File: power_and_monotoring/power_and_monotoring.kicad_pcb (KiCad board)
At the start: 2 copper layers, 122 x 177 mm, 149 parts, among them IC1 ADP3335ARMZ-5-R7, IC2 ADP3335ARMZ-3.3-RL, J1 Microfit_01x02_Vertical, J2 HLE-108-02-L-DV-BE-K-TR, J3 HLE-108-02-L-DV-BE-K-TR, J4 HLE-108-02-L-DV-BE-K-TR, J5 HLE-108-02-L-DV-BE-K-TR, K1 G5Q-1A, K2 G5Q-1A, K3 G5Q-1A, Q1 DMN6075SQ-7, U10 P783-Q24-S3-S, U11 CD4051BM96G3, U12 CD4051BM96G3, U2 LM7902D, U3 LM7902D, U4 LM7902D, U6 CD4081BM96, U7 CD4071BM96

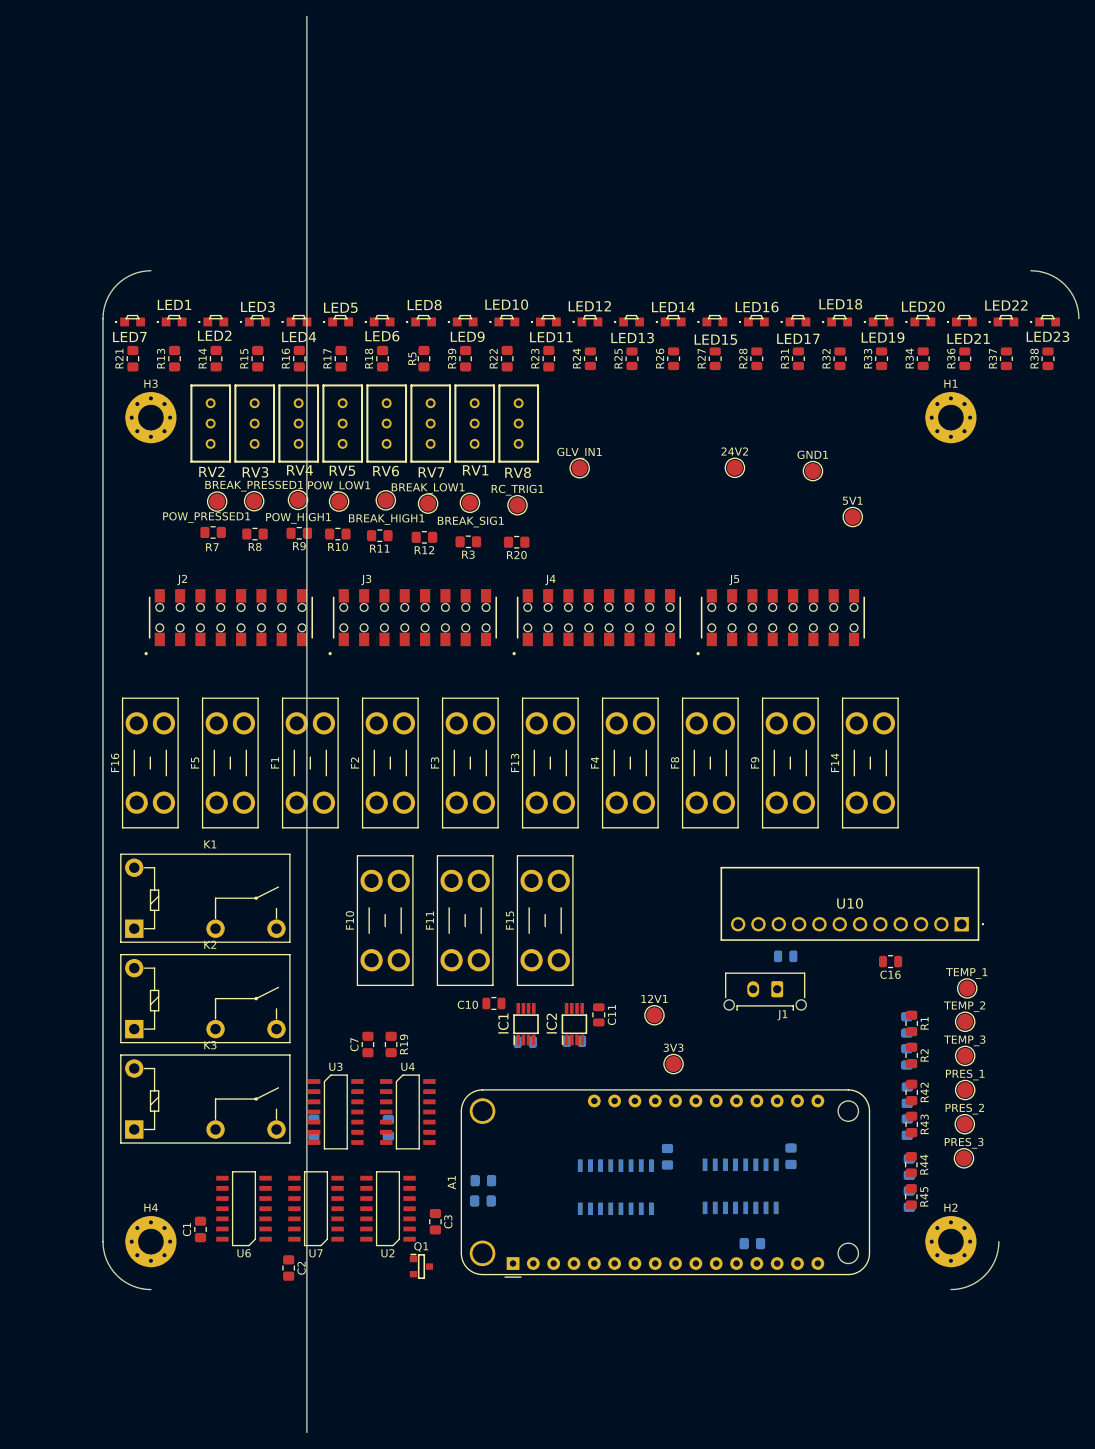
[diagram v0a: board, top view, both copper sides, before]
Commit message: first connections done (not perfect yet)
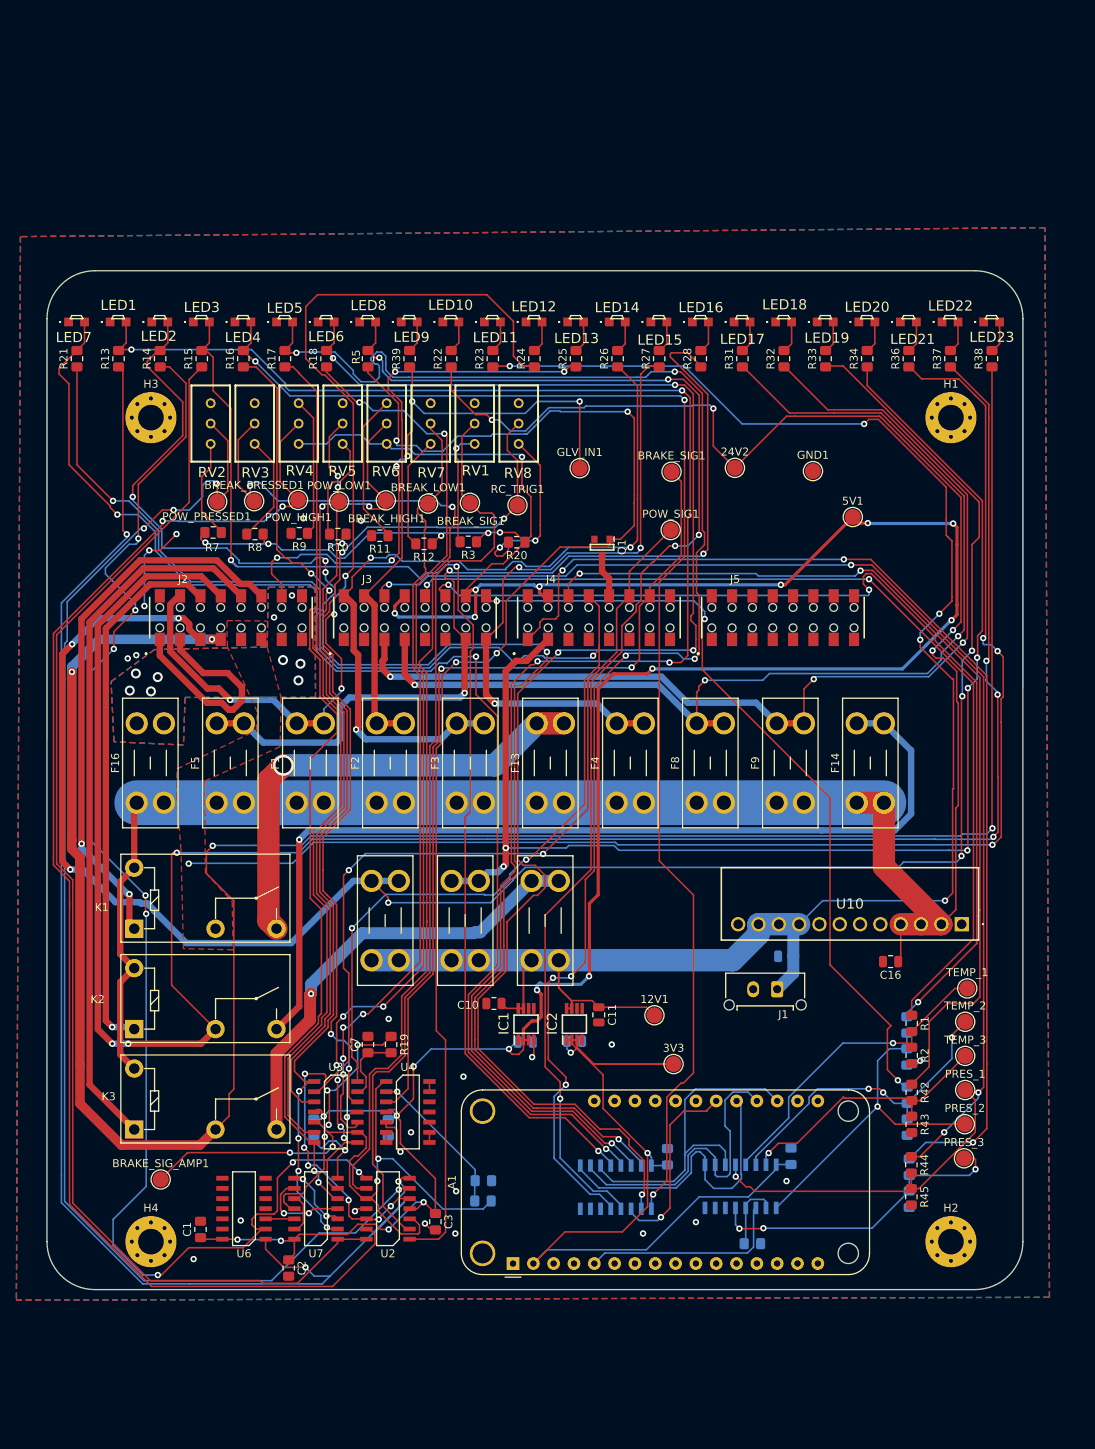
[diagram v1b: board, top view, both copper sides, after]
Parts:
- added BRAKE_SIG1: TestPoint, TestPoint:TestPoint_Pad_D2.0mm, F.Cu at (119.4, 151.9)
- added BRAKE_SIG_AMP1: TestPoint, TestPoint:TestPoint_Pad_D2.0mm, F.Cu at (55.5, 240.4)
- added POW_SIG1: TestPoint, TestPoint:TestPoint_Pad_D2.0mm, F.Cu at (119.3, 159.2)
- R24, R25, R26, R27, R28, R31, R32, R33, R34, R36, R37, R38: footprint Resistor_SMD:R_0805_2012Metric -> UniSA_Motorsport_Resistor:0805
- moved Q1 92.7 mm to (110.7, 161.4), turned to -90 degrees
- moved LED1 7.00 mm to (50.2, 133.2)
- moved LED10 7.00 mm to (91.8, 133.2)
- moved LED11 7.00 mm to (97.0, 133.2)
- moved LED12 7.00 mm to (102.2, 133.2)
- moved LED13 7.00 mm to (107.4, 133.2)
- moved LED14 7.00 mm to (112.6, 133.2)
- moved LED15 7.00 mm to (117.8, 133.2)
- moved LED17 7.00 mm to (128.2, 133.2)
- moved LED18 7.00 mm to (133.4, 133.2)
- moved LED19 7.00 mm to (138.6, 133.2)
- moved LED2 7.00 mm to (55.4, 133.2)
- moved LED20 7.00 mm to (143.8, 133.2)
- moved LED21 7.00 mm to (149.0, 133.2)
- moved LED22 7.00 mm to (154.2, 133.2)
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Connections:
- J2 pad 11: /Connectors/RADIATOR_FAN_24V -> /Connectors/RADIATOR_WATER_PUMP_24V
- J2 pad 8: /Connectors/RADIATOR_WATER_PUMP_24V -> /Connectors/RADIATOR_FAN_24V
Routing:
- net +5V: track 0.00 -> 394.6 mm, vias 0 -> 26
- net +24V: track 0.00 -> 301.6 mm, vias 0 -> 4
- net /Connectors/MC_12V: track 0.00 -> 289.3 mm, vias 0 -> 4
- net /Connectors/RADIATOR_FAN_24V: track 0.00 -> 275.3 mm, vias 0 -> 6
- net /Connectors/BRAKE_LIGHT_12V: track 0.00 -> 245.3 mm, vias 0 -> 7
- net +12V: track 0.00 -> 230.6 mm, vias 0 -> 5
- net /feather/POWER_SIG_HIGH: track 0.00 -> 208.4 mm, vias 0 -> 5
- net /feather/BRAKE_SIG_AMP_SHORT_GND: track 0.00 -> 192.8 mm, vias 0 -> 5
- net /feather/BRAKE_SIG_AMP_SHORT_HIGH: track 0.00 -> 189.1 mm, vias 0 -> 7
- net Net-(R13-Pad1): track 0.00 -> 186.0 mm, vias 0 -> 3
- net /feather/BRAKE_SIG_AMP_HIGH: track 0.00 -> 181.1 mm, vias 0 -> 5
- net /Connectors/BSPD_TRIGGER: track 0.00 -> 180.0 mm, vias 0 -> 4
- net Net-(R14-Pad1): track 0.00 -> 171.4 mm, vias 0 -> 8
- net /Connectors/RADIATOR_WATER_PUMP_24V: track 0.00 -> 170.6 mm, vias 0 -> 4
- net Net-(U2D--): track 0.00 -> 168.6 mm, vias 0 -> 2
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- added copper zone on B.Cu, net /Connectors/GLV_MASTER_SWITCH_OUT
- added copper zone on F.Cu, net /Connectors/GLV_MASTER_SWITCH_OUT
- added copper zone on F.Cu, net /Connectors/RADIATOR_WATER_PUMP_24V
- added copper zone on B.Cu, net GND
- added copper zone on F.Cu, net GND
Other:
- board size 122 x 177 mm -> 122 x 127.4 mm

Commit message: before design review
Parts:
- removed LED1, LED2, LED3, LED4, LED5, LED6, LED7: RED, LTST-S270KRKT, UniSA_Motorsport_Diode:0605
- removed LED10, LED11, LED12, LED13, LED14, LED15, LED16, LED17, LED18, LED19, LED20, LED21, LED22, LED23, LED8, LED9: GREEN, LTST-S270KGKT, UniSA_Motorsport_Diode:0605
- removed RV1, RV2, RV3, RV4, RV5, RV6, RV7, RV8: 10K, UniSA_Motorsport_Others:3296X_POT
- added D1: RED, UniSA_Motorsport_Diode:0805, F.Cu at (50.1, 134.2)
- added D10: GREEN, UniSA_Motorsport_Diode:0805, F.Cu at (92.0, 134.2)
- added D11: GREEN, UniSA_Motorsport_Diode:0805, F.Cu at (97.2, 134.2)
- added D12: GREEN, UniSA_Motorsport_Diode:0805, F.Cu at (102.4, 134.2)
- added D13: GREEN, UniSA_Motorsport_Diode:0805, F.Cu at (107.6, 134.2)
- added D14: GREEN, UniSA_Motorsport_Diode:0805, F.Cu at (112.8, 134.2)
- added D15: GREEN, UniSA_Motorsport_Diode:0805, F.Cu at (118.0, 134.2)
- added D16: GREEN, UniSA_Motorsport_Diode:0805, F.Cu at (123.2, 134.2)
- added D17: GREEN, UniSA_Motorsport_Diode:0805, F.Cu at (128.4, 134.2)
- added D18: GREEN, UniSA_Motorsport_Diode:0805, F.Cu at (133.6, 134.2)
- added D19: GREEN, UniSA_Motorsport_Diode:0805, F.Cu at (138.8, 134.2)
- added D2: RED, UniSA_Motorsport_Diode:0805, F.Cu at (55.6, 134.2)
- added D20: GREEN, UniSA_Motorsport_Diode:0805, F.Cu at (144.0, 134.2)
- added D21: GREEN, UniSA_Motorsport_Diode:0805, F.Cu at (149.2, 134.2)
- added D22: GREEN, UniSA_Motorsport_Diode:0805, F.Cu at (154.4, 134.2)
- added D23: GREEN, UniSA_Motorsport_Diode:0805, F.Cu at (159.6, 134.2)
- added D3: RED, UniSA_Motorsport_Diode:0805, F.Cu at (60.8, 134.2)
- added D4: RED, UniSA_Motorsport_Diode:0805, F.Cu at (66.0, 134.2)
- added D5: RED, UniSA_Motorsport_Diode:0805, F.Cu at (71.2, 134.2)
- added D6: RED, UniSA_Motorsport_Diode:0805, F.Cu at (76.4, 134.2)
- added D7: RED, UniSA_Motorsport_Diode:0805, F.Cu at (44.6, 134.2)
- added D8: GREEN, UniSA_Motorsport_Diode:0805, F.Cu at (81.6, 134.2)
- added D9: GREEN, UniSA_Motorsport_Diode:0805, F.Cu at (86.8, 134.2)
- added J6: 43045-1015, UniSA_Motorsport_Connector:MOLEX_43045-10YY_10PIN, F.Cu at (151.4, 168.8)
- added J7: 43045-1615, UniSA_Motorsport_Connector:MOLEX_43045-16YY_16PIN, F.Cu at (131.0, 150.4)
- added RL1: 10 K, UniSA_Motorsport_Resistor:3296W-1, F.Cu at (61.7, 145.9)
- added RL2: 10 K, UniSA_Motorsport_Resistor:3296W-1, F.Cu at (67.3, 145.9)
- added RL3: 10 K, UniSA_Motorsport_Resistor:3296W-1, F.Cu at (72.9, 146.0)
- added RL4: 10 K, UniSA_Motorsport_Resistor:3296W-1, F.Cu at (78.2, 146.0)
- added RL5: 10 K, UniSA_Motorsport_Resistor:3296W-1, F.Cu at (83.7, 145.8)
- added RL6: 10 K, UniSA_Motorsport_Resistor:3296W-1, F.Cu at (89.6, 145.9)
- added RL7: 10 K, UniSA_Motorsport_Resistor:3296W-1, F.Cu at (100.5, 146.0)
- added RL8: 10 K, UniSA_Motorsport_Resistor:3296W-1, F.Cu at (95.0, 145.9)
- moved 5V1 27.8 mm to (153.0, 183.1)
- moved 24V2 17.7 mm to (110.0, 147.6)
- moved GND1 15.6 mm to (152.6, 153.6)
- moved BRAKE_SIG1 8.24 mm to (111.2, 152.3)
- moved Q1 3.59 mm to (110.8, 157.8)
- moved R12 1.83 mm to (88.6, 159.1)
- moved R3 1.08 mm to (94.1, 159.6)
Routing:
- net /feather/D_BSPD_TRIGGER: track 165.2 -> 310.6 mm, vias 3 -> 5
- net /feather/BRAKE_LIGHT_SIG: track 164.6 -> 247.8 mm, vias 5 -> 6
- net /feather/BRAKE_SIG_AMP_SHORT_HIGH: track 189.1 -> 269.3 mm, vias 7 -> 10
- net /feather/POWER_SIG_SHORT_GND: track 168.2 -> 241.5 mm, vias 3 -> 7
- net /feather/BRAKE_SIG_AMP_SHORT_GND: track 192.8 -> 265.4 mm, vias 5 -> 6
- net /feather/POWER_SIG_HIGH: track 208.4 -> 279.3 mm, vias 5 -> 6
- net /feather/POWER_SIG_SHORT_HIGH: track 149.5 -> 211.2 mm, vias 3 -> 5
- net /Connectors/BSPD_TEST_12V: track 164.1 -> 113.6 mm
- net /feather/BRAKE_SIG_AMP_HIGH: track 181.1 -> 231.4 mm, vias 5 -> 6
- net /Connectors/SAFETY_24V: track 74.0 -> 122.0 mm, vias 2 -> 3
- net /Connectors/AIR_24V: track 123.9 -> 171.1 mm, vias 4 -> 8
- net /Connectors/ECU_24V: track 139.4 -> 98.8 mm
- net /Connectors/MC_12V: track 289.3 -> 324.4 mm, vias 4 -> 7
- net /Connectors/RADIATOR_FAN_24V: track 275.3 -> 306.5 mm
- net /Connectors/BRAKE_LIGHT_12V: track 245.3 -> 273.2 mm, vias 7 -> 8
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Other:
- board size 122 x 127.4 mm -> 122 x 124.4 mm
- board text added: "12 Break light"
- board text added: "12V motor controller"
- board text added: "AIR 24V"
- board text added: "B1-1"
- board text added: "B1-10"
- board text added: "B1-11"
- board text added: "B1-12"
- board text added: "B1-13"
- board text added: "B1-14"
- board text added: "B1-15"
- board text added: "B1-16"
- board text added: "B1-2"
- board text added: "B1-3"
- board text added: "B1-4"
- board text added: "B1-5"
- board text added: "B1-6"
- board text added: "B1-7"
- board text added: "B1-8"
- board text added: "B1-9"
- board text added: "B2-1"
- board text added: "B2-10"
- board text added: "B2-11"
- board text added: "B2-12"
- board text added: "B2-13"
- board text added: "B2-14"
- board text added: "B2-15"
- board text added: "B2-16"
- board text added: "B2-2"
- board text added: "B2-3"
- board text added: "B2-4"
- board text added: "B2-5"
- board text added: "B2-6"
- board text added: "B2-7"
- board text added: "B2-8"
- board text added: "B2-9"
- board text added: "B3-1"
- board text added: "B3-10"
- board text added: "B3-11"
- board text added: "B3-12"
- board text added: "B3-13"
- board text added: "B3-14"
- board text added: "B3-15"
- board text added: "B3-16"
- board text added: "B3-2"
- board text added: "B3-3"
- board text added: "B3-4"
- board text added: "B3-5"
- board text added: "B3-6"
- board text added: "B3-7"
- board text added: "B3-8"
- board text added: "B3-9"
- board text added: "B4-1"
- board text added: "B4-10"
- board text added: "B4-11"
- board text added: "B4-12"
- board text added: "B4-13"
- board text added: "B4-14"
- board text added: "B4-15"
- board text added: "B4-16"
- board text added: "B4-2"
- board text added: "B4-3"
- board text added: "B4-4"
- board text added: "B4-5"
- board text added: "B4-6"
- board text added: "B4-7"
- board text added: "B4-8"
- board text added: "B4-9"
- board text added: "BSPD 12V"
- board text added: "Dash 24V"
- board text added: "ECU 24V"
- board text added: "GLV IN"
- board text added: "HV BOX 24V"
- board text added: "M ACC 24V"
- board text added: "POWER SIG"
- board text added: "Radiator Pump"
- board text added: "Radiator fan"
- board text added: "S ACC 24V"
- board text added: "SAFTEY 24V"

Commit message: Final
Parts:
- removed C1: GCM0805_1u, UniSA_Motorsport_Capacitor:0805
- removed C16, C17: C, Capacitor_SMD:C_0805_2012Metric
- removed R10, R11, R12, R20, R35, R41, R42, R43, R9: CRCW0805, UniSA_Motorsport_Resistor:0805
- removed U10: P783-Q24-S3-S, UniSA_Motorsport_Others:P783-Q24-S3-S
- removed U6: CD4081BM96, UniSA_Motorsport_SO:SOIC-14
- added C6: 100uF, UniSA_Motorsport_Capacitor:EEEFK0J332AQ, F.Cu at (146.2, 206.2)
- added C8: EEV-FK1H391Q, UniSA_Motorsport_Capacitor:EEEFK0J332AQ, F.Cu at (127.3, 206.7)
- added D24: 1N4148W RHG, UniSA_Motorsport_Diode:SOD-123F-2, F.Cu at (74.7, 203.2)
- added D25: 1N4148W RHG, UniSA_Motorsport_Diode:SOD-123F-2, F.Cu at (74.8, 210.2)
- added D26: 1N4148W RHG, UniSA_Motorsport_Diode:SOD-123F-2, F.Cu at (48.8, 241.4)
- added D27: NRVTS245ESFT1G, UniSA_Motorsport_Diode:SOD-123FL-2, F.Cu at (119.3, 222.9)
- added D28: MMBZ5225BS-7-F, UniSA_Motorsport_SOT_TO:SOT-363, B.Cu at (99.3, 236.6)
- added D29: MMBZ5225BS-7-F, UniSA_Motorsport_SOT_TO:SOT-363, B.Cu at (101.2, 227.0)
- added D30: MMBZ5225BS-7-F, UniSA_Motorsport_SOT_TO:SOT-363, B.Cu at (122.8, 219.0)
- added D31: MMBZ5225BS-7-F, UniSA_Motorsport_SOT_TO:SOT-363, B.Cu at (122.7, 215.8)
- added IC3: LM2576-12WU-TR, UniSA_Motorsport_SO:TO-263-5, F.Cu at (145.4, 221.1)
- added L1: 100uH, UniSA_Motorsport_Inductor:5050, F.Cu at (128.0, 222.1)
- added R29: CRCW0805, UniSA_Motorsport_Resistor:0805, F.Cu at (88.0, 238.3)
- added R30: CRCW0805, UniSA_Motorsport_Resistor:0805, F.Cu at (89.6, 241.1)
- added R50: CRCW0805, UniSA_Motorsport_Resistor:0805, F.Cu at (93.4, 227.0)
- added R51: CRCW0805, UniSA_Motorsport_Resistor:0805, F.Cu at (93.4, 229.3)
- added RN1: EXB-38V103JV, UniSA_Motorsport_Resistor:EXB38V472JV, F.Cu at (92.8, 220.3)
- added RN2: EXB-38V103JV, UniSA_Motorsport_Resistor:EXB38V472JV, F.Cu at (114.6, 214.8)
- added U1: 74LVC1G08GW,125, UniSA_Motorsport_SO:TSSOP-5, F.Cu at (66.9, 250.9)
- R1, R2, R8: moved to B.Cu
- moved R8 110.2 mm to (147.1, 235.7), turned to 0 degrees
- moved POW_SIG_AMP1 100.1 mm to (59.8, 239.8)
- moved R7 83.7 mm to (68.4, 243.0), turned to 90 degrees
- moved R3 61.8 mm to (83.8, 220.5)
- moved BRAKE_SIG_AMP1 31.7 mm to (84.8, 252.5)
- moved R46 25.2 mm to (160.7, 243.3)
- moved R47 25.2 mm to (160.7, 247.3)
- moved J1 22.2 mm to (113.8, 204.8), turned to -90 degrees
- moved TEMP_2 16.2 mm to (150.8, 236.0)
- moved TEMP_3 16.2 mm to (150.8, 240.2)
- moved TEMP_1 16.2 mm to (151.0, 231.8)
- moved R2 14.9 mm to (143.8, 238.7), turned to 0 degrees
- moved R1 11.4 mm to (147.4, 232.2), turned to 0 degrees
- moved 12V1 7.90 mm to (116.6, 227.7)
- moved 3V3 6.81 mm to (113.0, 227.6)
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- renumbered D7 to D1, D1 to D2, D2 to D3, D3 to D4, D4 to D5, D5 to D6, D6 to D7, POW_SIG1 to POW_SIG_AMP1
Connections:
- C5 pad 1: +5V -> +12V
- D1 pad 2: /feather/D_BSPD_TRIGGER -> Net-(D1-A)
- D2 pad 2: /feather/POWER_SIG_HIGH -> Net-(D2-A)
- D3 pad 2: /feather/BRAKE_SIG_AMP_HIGH -> Net-(D3-A)
- D4 pad 2: /feather/POWER_SIG_SHORT_HIGH -> Net-(D4-A)
- D5 pad 2: /feather/POWER_SIG_SHORT_GND -> Net-(D5-A)
- D6 pad 2: /feather/BRAKE_SIG_AMP_SHORT_HIGH -> Net-(D6-A)
- D7 pad 2: /feather/BRAKE_SIG_AMP_SHORT_GND -> Net-(D7-A)
- D8 pad 2: /feather/BRAKE_LIGHT_SIG -> Net-(D8-A)
- J6 pad 7: /feather/D_BSPD_TRIGGER -> /Connectors/BSPD_TRIGGER
- POW_SIG_AMP1 pad 1: /Connectors/POWER_SIGNAL -> /logic/POW_SIG_AMP
- Q1 pad 1: Net-(Q1-G) -> /feather/BRAKE_LIGHT_SIG
- R1 pad 1: /Connectors/PRESSURE/TEMP_SENSOR_1_TEMP -> +3V3
- R1 pad 2: Net-(U12-X0) -> /Connectors/PRESSURE/TEMP_SENSOR_1_TEMP
- R13 pad 1: Net-(R13-Pad1) -> /feather/POWER_SIG_HIGH
- R13 pad 2: /feather/POWER_SIG_HIGH -> Net-(D2-A)
- R14 pad 1: Net-(R14-Pad1) -> /feather/BRAKE_SIG_AMP_HIGH
- R14 pad 2: /feather/BRAKE_SIG_AMP_HIGH -> Net-(D3-A)
- R15 pad 1: Net-(R15-Pad1) -> /feather/POWER_SIG_SHORT_HIGH
- R15 pad 2: /feather/POWER_SIG_SHORT_HIGH -> Net-(D4-A)
- R16 pad 1: Net-(R16-Pad1) -> /feather/POWER_SIG_SHORT_GND
- R16 pad 2: /feather/POWER_SIG_SHORT_GND -> Net-(D5-A)
- R17 pad 1: Net-(R17-Pad1) -> /feather/BRAKE_SIG_AMP_SHORT_HIGH
- R17 pad 2: /feather/BRAKE_SIG_AMP_SHORT_HIGH -> Net-(D6-A)
- R18 pad 1: Net-(R18-Pad1) -> /feather/BRAKE_SIG_AMP_SHORT_GND
- R18 pad 2: /feather/BRAKE_SIG_AMP_SHORT_GND -> Net-(D7-A)
- R2 pad 1: Net-(U12-X0) -> +3V3
- R2 pad 2: GND -> /Connectors/PRESSURE/TEMP_SENSOR_3_TEMP
- R21 pad 2: /feather/D_BSPD_TRIGGER -> Net-(D1-A)
- R3 pad 1: +5V -> Net-(R19-Pad1)
- R3 pad 2: Net-(R3-Pad2) -> GND
- R5 pad 1: Net-(Q1-G) -> /feather/BRAKE_LIGHT_SIG
- R5 pad 2: /feather/BRAKE_LIGHT_SIG -> Net-(D8-A)
- R6 pad 1: /logic/BRAKE_SIG_AMP -> Net-(R50-Pad1)
- R7 pad 1: +5V -> Net-(R7-Pad1)
- R7 pad 2: Net-(R7-Pad2) -> Net-(R19-Pad1)
- R8 pad 1: +5V -> +3V3
- R8 pad 2: Net-(R8-Pad2) -> /Connectors/PRESSURE/TEMP_SENSOR_2_TEMP
- RL1 pad 1: Net-(R7-Pad2) -> +3V3
- RL2 pad 1: Net-(R8-Pad2) -> +3V3
- RL3 pad 1: +5V -> +3V3
- RL3 pad 3: Net-(R9-Pad1) -> GND
- RL4 pad 1: Net-(R10-Pad2) -> +3V3
- RL5 pad 1: +5V -> +3V3
- RL5 pad 3: Net-(R11-Pad1) -> GND
- RL6 pad 1: Net-(R12-Pad2) -> +3V3
- RL7 pad 1: Net-(R20-Pad2) -> +3V3
- RL8 pad 1: Net-(R3-Pad2) -> +3V3
- TEMP_1 pad 1: Net-(U12-X0) -> /Connectors/PRESSURE/TEMP_SENSOR_1_TEMP
- TEMP_2 pad 1: Net-(U12-X1) -> /Connectors/PRESSURE/TEMP_SENSOR_2_TEMP
- TEMP_3 pad 1: Net-(U12-X2) -> /Connectors/PRESSURE/TEMP_SENSOR_3_TEMP
- U11 pad 1: /feather/POWER_SIG_SHORT_GND -> Net-(U11-X4)
- U11 pad 12: /feather/POWER_SIG_SHORT_HIGH -> Net-(U11-X3)
- U11 pad 13: /feather/D_BSPD_TRIGGER -> Net-(U11-X0)
- U11 pad 14: /feather/POWER_SIG_HIGH -> Net-(U11-X1)
- U11 pad 15: /feather/BRAKE_SIG_AMP_HIGH -> Net-(U11-X2)
- U11 pad 2: /feather/BRAKE_SIG_AMP_SHORT_GND -> Net-(U11-X6)
- U11 pad 4: /feather/BRAKE_LIGHT_SIG -> Net-(U11-X7)
- U11 pad 5: /feather/BRAKE_SIG_AMP_SHORT_HIGH -> Net-(U11-X5)
- U12 pad 13: Net-(U12-X0) -> /Connectors/PRESSURE/TEMP_SENSOR_1_TEMP
- U12 pad 14: Net-(U12-X1) -> /Connectors/PRESSURE/TEMP_SENSOR_2_TEMP
- U12 pad 15: Net-(U12-X2) -> /Connectors/PRESSURE/TEMP_SENSOR_3_TEMP
- U2 pad 1: Net-(Q1-G) -> /feather/BRAKE_LIGHT_SIG
- U2 pad 12: /Connectors/POWER_SIGNAL -> /logic/POW_SIG_AMP
- U2 pad 14: Net-(R15-Pad1) -> /feather/POWER_SIG_SHORT_HIGH
- U2 pad 5: /Connectors/POWER_SIGNAL -> /logic/POW_SIG_AMP
- U2 pad 7: Net-(R13-Pad1) -> /feather/POWER_SIG_HIGH
- U2 pad 8: Net-(R14-Pad1) -> /feather/BRAKE_SIG_AMP_HIGH
- U3 pad 1: Net-(R16-Pad1) -> /feather/POWER_SIG_SHORT_GND
- U3 pad 2: /Connectors/POWER_SIGNAL -> /logic/POW_SIG_AMP
- U3 pad 7: Net-(R17-Pad1) -> /feather/BRAKE_SIG_AMP_SHORT_HIGH
- U3 pad 8: Net-(R18-Pad1) -> /feather/BRAKE_SIG_AMP_SHORT_GND
- U4 pad 1: /logic/BRAKE_SIG_AMP -> Net-(R50-Pad1)
- U4 pad 10: GND -> Net-(U4C-+)
- U4 pad 12: GND -> Net-(U4D-+)
- U4 pad 13: Net-(U4D--) -> /logic/BRAKE_SIG_AMP
- U4 pad 14: Net-(U4D--) -> /logic/BRAKE_SIG_AMP
- U4 pad 4: +5V -> +12V
- U4 pad 5: GND -> /Connectors/POWER_SIGNAL
- U4 pad 8: Net-(U4C--) -> /logic/POW_SIG_AMP
- U4 pad 9: Net-(U4C--) -> /logic/POW_SIG_AMP
- U7 pad 1: Net-(R15-Pad1) -> /feather/POWER_SIG_SHORT_HIGH
- U7 pad 11: Net-(R19-Pad1) -> Net-(R7-Pad1)
- U7 pad 2: Net-(R16-Pad1) -> /feather/POWER_SIG_SHORT_GND
- U7 pad 5: Net-(R17-Pad1) -> /feather/BRAKE_SIG_AMP_SHORT_HIGH
- U7 pad 6: Net-(R18-Pad1) -> /feather/BRAKE_SIG_AMP_SHORT_GND
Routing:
- net /feather/D_BSPD_TRIGGER: track 310.6 -> 0.00 mm, vias 5 -> 0
- net /Connectors/BSPD_TRIGGER: track 180.0 -> 381.9 mm, vias 4 -> 8
- net Net-(R13-Pad1): track 186.0 -> 0.00 mm, vias 3 -> 0
- net Net-(R14-Pad1): track 171.4 -> 0.00 mm, vias 8 -> 0
- net Net-(Q1-G): track 164.7 -> 0.00 mm, vias 4 -> 0
- net Net-(R15-Pad1): track 156.3 -> 0.00 mm
- net +3V3: track 101.3 -> 256.6 mm, vias 2 -> 9
- net /feather/POWER_SIG_HIGH: track 279.3 -> 425.1 mm, vias 6 -> 8
- net /feather/BRAKE_LIGHT_SIG: track 247.8 -> 377.1 mm, vias 6 -> 11
- net Net-(R18-Pad1): track 126.7 -> 0.00 mm, vias 8 -> 0
- net Net-(R16-Pad1): track 125.8 -> 0.00 mm, vias 6 -> 0
- net Net-(R17-Pad1): track 115.4 -> 0.00 mm, vias 2 -> 0
- net +5V: track 369.0 -> 253.9 mm, vias 25 -> 16
- net /feather/BRAKE_SIG_AMP_HIGH: track 231.4 -> 341.5 mm, vias 6 -> 13
- net /feather/POWER_SIG_SHORT_HIGH: track 211.2 -> 318.4 mm, vias 5 -> 4
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- added copper zone on F.Cu, net +12V
- added copper zone on B.Cu, net +24V
- added copper zone on F.Cu, net +24V
- added copper zone on F.Cu, net /voltage_reg/Reg_out
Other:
- board text added: "12V"
- board text added: "24V"
- board text added: "24_RAD_FAN"
- board text added: "24_RAD_PUMP"
- board text added: "AIR_POWER"
- board text added: "BRAKE_HIGH"
- board text added: "BRAKE_LIGHT"
- board text added: "BRAKE_SHORT_GND"
- board text added: "BRAKE_SHORT_HIGH"
- board text added: "BREAK_LIGHT_12V"
- board text added: "BSPD_12V"
- board text added: "BSPD_TRIG"
- board text added: "DASH_24V"
- board text added: "ECU_24V"
- board text added: "GLV_IN"
- board text added: "HV_BOX_24V"
- board text added: "MAS_ACC_24V"
- board text added: "MOT_CONT_24V"
- board text added: "POWER SIG AMP"
- board text added: "POW_SHORT_GND"
- board text added: "POW_SHORT_HIGH"
- board text added: "POW_SIG_HIGH"
- board text added: "SAFTEY_24V"
- board text added: "SLAV_ACC_24V"
- board text removed: "POWER SIG"
